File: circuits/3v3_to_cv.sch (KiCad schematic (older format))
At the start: 17 parts, among them U2 TL074CDT, U3 LM324

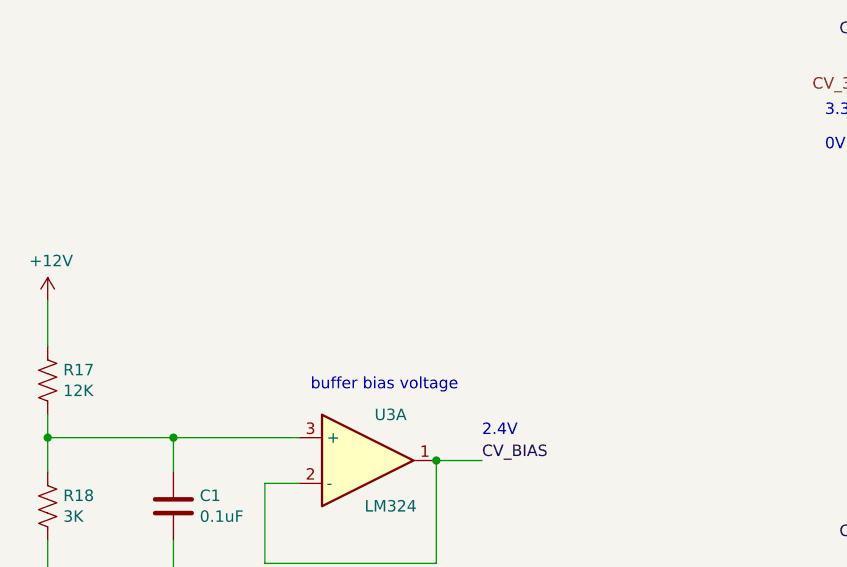
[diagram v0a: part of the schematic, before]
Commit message: updating circuit fragements with simulation links and fixing bugs
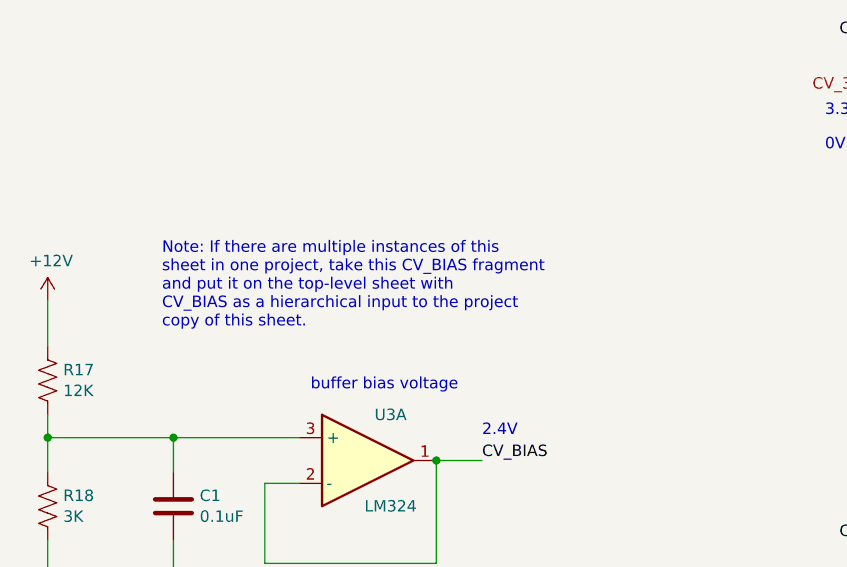
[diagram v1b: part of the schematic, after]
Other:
- note added: "Note: If there are multiple instances of this\nsheet in one project, take this CV_BIAS fragment\nand put it on the top-level sheet with\nCV_BIAS as a hierarchical input to the project\ncopy of this sheet."
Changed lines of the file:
@@
 	1    0    0    -1
 $EndComp
+Text Notes 1600 4575 0    50   ~ 0
+Note: If there are multiple instances of this\nsheet in one project, take this CV_BIAS fragment\nand put it on the top-level sheet with\nCV_BIAS as a hierarchical input to the project\ncopy of this sheet.
 $EndSCHEMATC
